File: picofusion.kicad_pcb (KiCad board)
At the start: 4 copper layers, 25.5 x 25.5 mm, 102 parts, among them J1 NORTH, J2 EAST, J3 WEST, J4 SOUTH, U1 W25Q16, U2 RP2040, U3 TLV71333PDQN, U4 ICM42605, U5 MMC5983MA, U6 ICP20100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

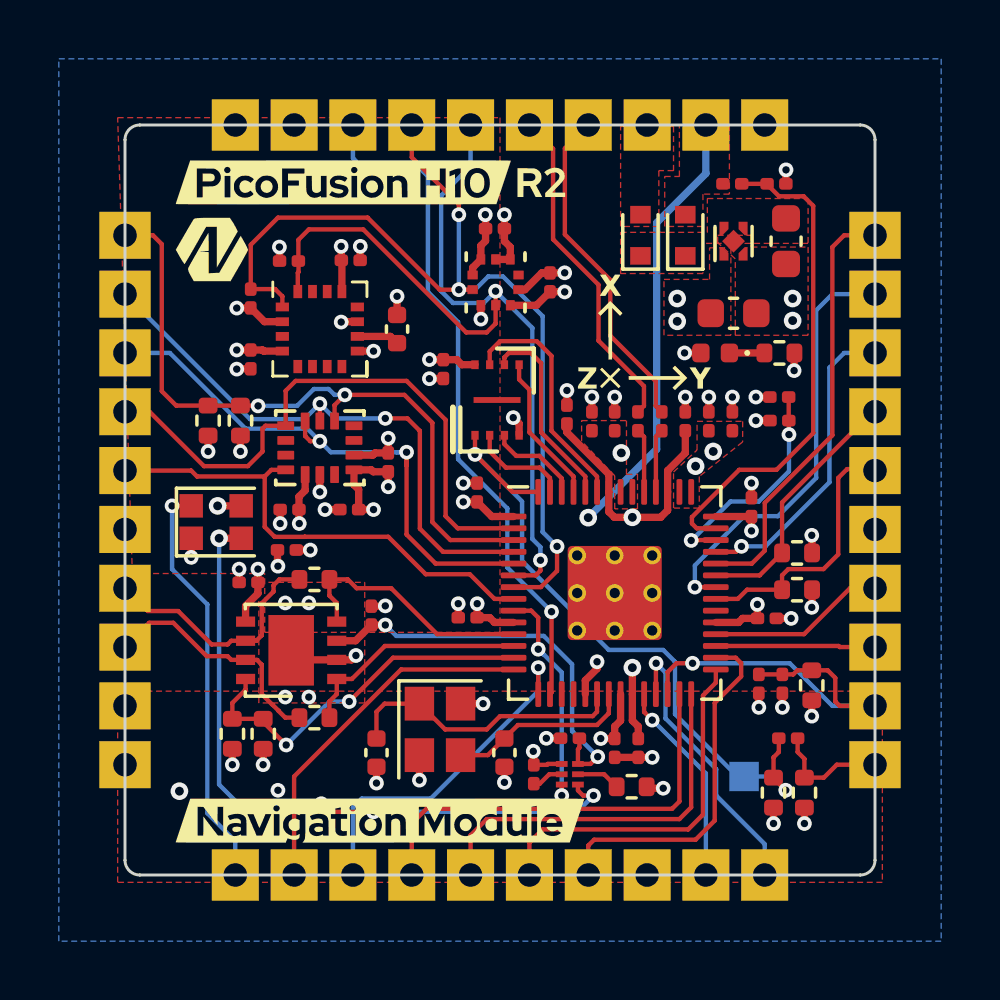
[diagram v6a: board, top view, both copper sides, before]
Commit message: schematic: reformat and R3 release candidate
* reformat schematic
* minor fixes from R2 testing
* no functionality differences
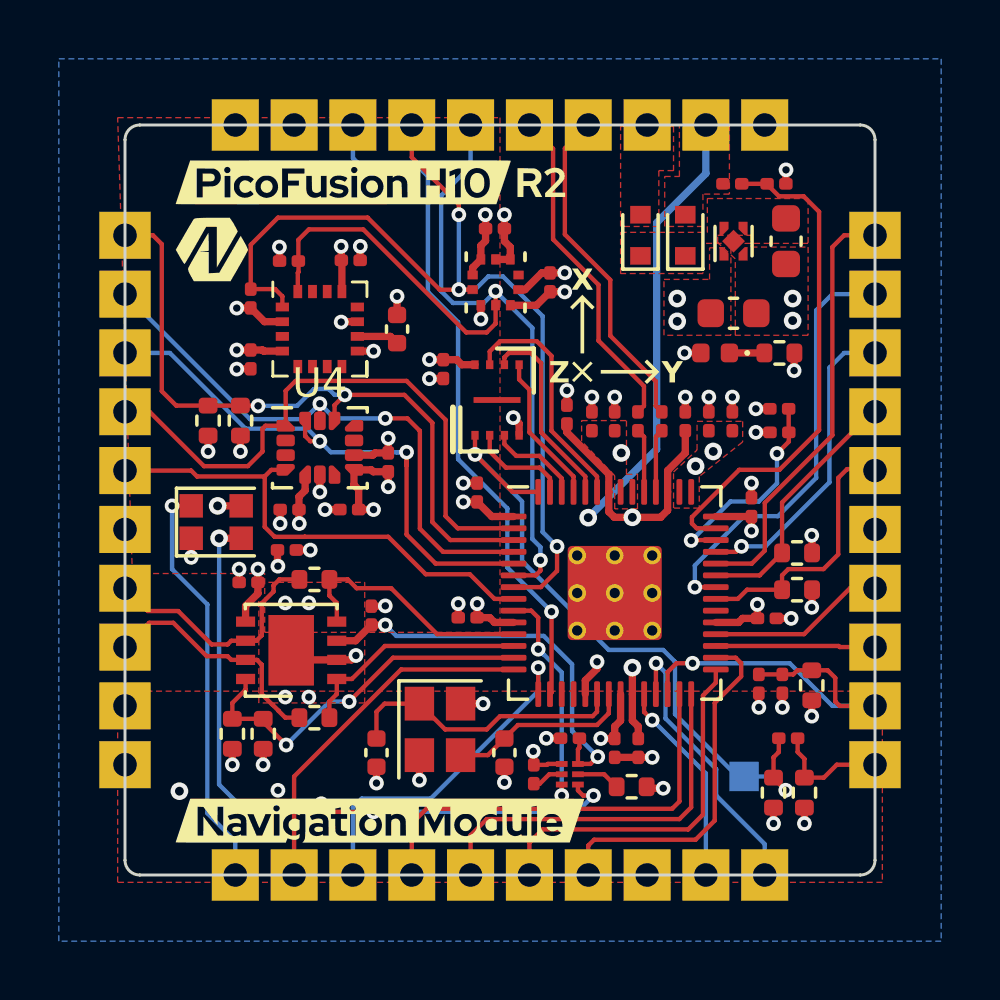
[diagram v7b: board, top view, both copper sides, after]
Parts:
- R6: value 470 -> 1.5K
- U4: footprint ICM-42605:PQFN50P300X250X97-14N -> Package_LGA:LGA-14_3x2.5mm_P0.5mm_LayoutBorder3x4y
- moved G*** 0.97 mm to (164.1, 34.4)
- moved R22 0.40 mm to (169.5, 37.7)
- moved R17 0.40 mm to (169.5, 36.9)
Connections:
- net /5V_RECT renamed Net-(C14-Pad1)
- net /LED_3V3 renamed /NEOPIXEL_3V3
- net /NEOPIXEL renamed Net-(D4-Pad3)
- net /QSPI_SCLK renamed /QSPI_SCK
- R15 pad 1: +5V -> +3V3
- R15 pad 2: /5V_SENSE -> /3V3_SENSE
- R16 pad 1: /5V_SENSE -> /3V3_SENSE
- R17 pad 1: +3V3 -> +5V
- R17 pad 2: /3V3_SENSE -> /5V_SENSE
- R22 pad 1: /3V3_SENSE -> /5V_SENSE
- U4 pad 10: unconnected-(U4-Pad10) -> (no net)
- U4 pad 11: unconnected-(U4-Pad11) -> (no net)
- U4 pad 2: unconnected-(U4-Pad2) -> (no net)
- U4 pad 3: unconnected-(U4-Pad3) -> (no net)
- U4 pad 7: unconnected-(U4-Pad7) -> (no net)
- U5 pad 12: (no net) -> unconnected-(U5-Pad12)
- U5 pad 14: (no net) -> unconnected-(U5-Pad14)
- U5 pad 3: (no net) -> unconnected-(U5-Pad3)
- U5 pad 6: (no net) -> unconnected-(U5-Pad6)
- U5 pad 7: (no net) -> unconnected-(U5-Pad7)
- U5 pad 8: (no net) -> unconnected-(U5-Pad8)
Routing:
- net /5V_SENSE: track 16.9 -> 7.27 mm, vias 0 -> 2
- net /3V3_SENSE: track 7.67 -> 17.1 mm, vias 2 -> 0
- net +5V: track 49.3 -> 49.8 mm, vias 5 -> 6
- net +3V3: track 33.9 -> 33.4 mm, vias 30 -> 29

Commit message: schematic: more improvements towards R3
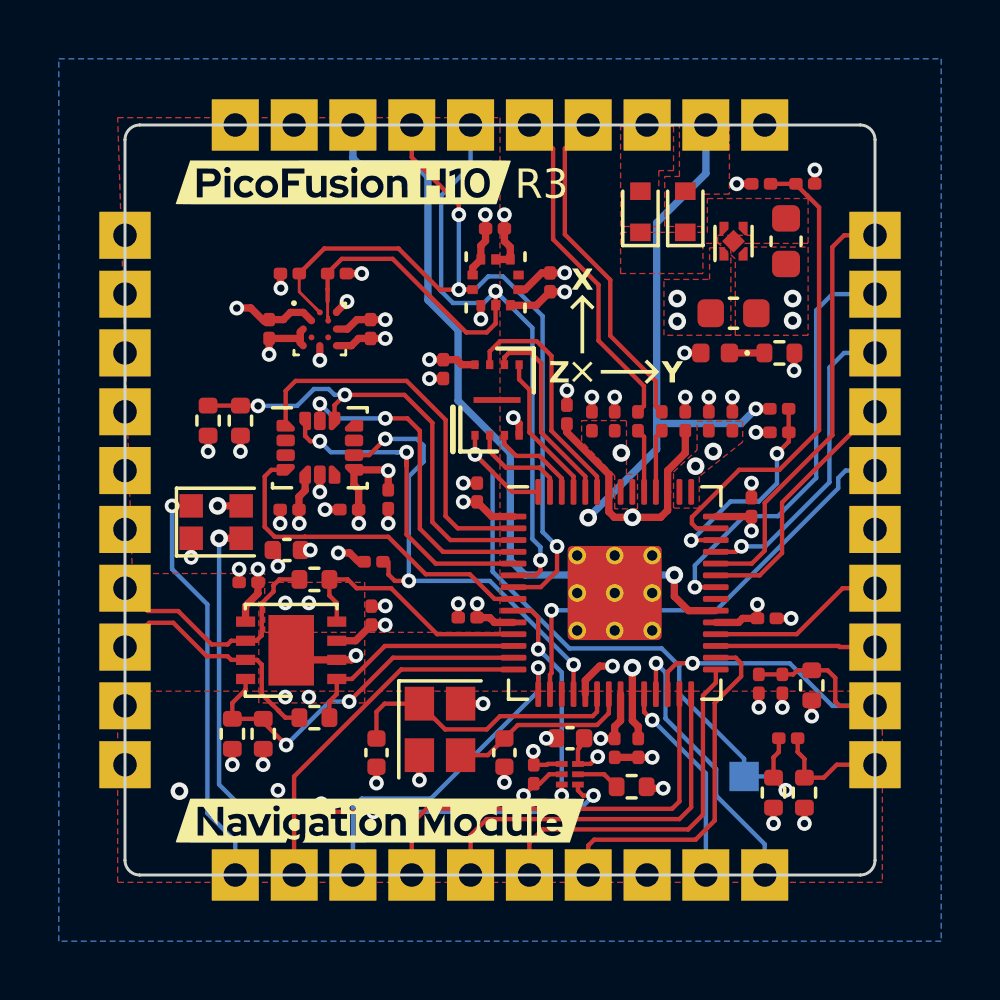
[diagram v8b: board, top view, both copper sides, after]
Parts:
- removed C12: 1uF, Capacitor_SMD:C_0201_0603Metric
- removed C20: 10uF, Capacitor_SMD:C_0402_1005Metric
- removed C21: 0.1uF, Capacitor_SMD:C_0201_0603Metric
- removed the G*** at (150.2, 31.5)
- removed the G*** at (157.0, 44.7)
- removed the G*** at (170.5, 29.2)
- removed R4, R5: 10K, Resistor_SMD:R_0402_1005Metric
- added C32: 0u1, Capacitor_SMD:C_0201_0603Metric, F.Cu at (152.2, 34.2)
- added C33: 0u1, Capacitor_SMD:C_0201_0603Metric, F.Cu at (155.6, 34.2)
- added R24: 10K, Resistor_SMD:R_0201_0603Metric, F.Cu at (155.7, 42.1)
- C1, C10, C11, C13, C14, C15, C16, C18, C2, C22, C23, C24, C26, C27, C28, C29, C4, C6, C7, C9: value 0.1uF -> 0u1
- C17: value 2.2uF -> 2u2
- C19: value 10nF -> 10n
- C25, C3: value 1uF -> 1u
- C30: value 0.1uF -> 0u1; footprint Capacitor_SMD:C_0201_0603Metric -> Capacitor_SMD:C_0402_1005Metric
- C31: value 1uF -> 1u; footprint Capacitor_SMD:C_0201_0603Metric -> Capacitor_SMD:C_0402_1005Metric
- C5, C8: value 10pF -> 10p
- R6, R8, R9: value 1.5K -> 1K5
- U4: value ICM42605 -> ICM-42688-P
- U5: value MMC5983MA -> BMM150; footprint Package_LGA:LGA-16_3x3mm_P0.5mm -> Package_CSP:WLCSP-12_1.56x1.56mm_P0.4mm
- moved R9 1.69 mm to (154.5, 32.3), turned to 180 degrees
- moved R8 1.58 mm to (152.9, 32.3), turned to 0 degrees
- moved C18 1.26 mm to (156.2, 40.0), turned to 90 degrees
- moved R15 0.98 mm to (168.9, 29.2)
- moved R16 0.98 mm to (170.4, 29.2)
- moved D1 0.80 mm to (166.3, 30.2)
- moved D3 0.80 mm to (164.8, 30.2)
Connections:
- net /SPI1_PICO_SD renamed /SPI1_MOSI
- net /SPI1_POCI_SD renamed /SPI1_MISO
- net /SPI1_SCK_SD renamed /SPI1_SCK
- net /SPI1_nCS_SD renamed /SPI1_nCS
- J1 pad 3: /RESV1 -> /USB_VBUS
- J2 pad 5: /SD_nCD -> /RESV1
- J3 pad 1: /SPI0_nCS -> unconnected-(J3-Pin_1-Pad1)
- J3 pad 2: /SPI0_SCK -> unconnected-(J3-Pin_2-Pad2)
- J3 pad 3: /SPI0_PICO -> unconnected-(J3-Pin_3-Pad3)
- J3 pad 4: /SPI0_POCI -> unconnected-(J3-Pin_4-Pad4)
- J3 pad 5: /DRDY_ICM42605 -> unconnected-(J3-Pin_5-Pad5)
- U2 pad 18: unconnected-(U2-Pad18) -> /PWM7B_FSYNC
- U2 pad 2: /SPI0_POCI -> /SPI0_MISO
- U2 pad 34: unconnected-(U2-Pad34) -> /USB_VBUS
- U2 pad 35: /SD_nCD -> unconnected-(U2-GPIO23-Pad35)
- U2 pad 40: /3V3_SENSE -> /5V_SENSE
- U2 pad 41: /5V_SENSE -> /3V3_SENSE
- U2 pad 5: /SPI0_PICO -> /SPI0_MOSI
- U2 pad 8: /DRDY_ICM42605 -> /DRDY_ICM42688P
- U4 pad 1: /SPI0_POCI -> /SPI0_MISO
- U4 pad 14: /SPI0_PICO -> /SPI0_MOSI
- U4 pad 4: /DRDY_ICM42605 -> /DRDY_ICM42688P
- U4 pad 9: GND -> /PWM7B_FSYNC
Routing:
- net /USB_VBUS: track 0.00 -> 26.2 mm, vias 0 -> 1
- net /SPI0_POCI: track 20.2 -> 0.00 mm
- net /SPI0_PICO: track 19.6 -> 0.00 mm, vias 2 -> 0
- net /DRDY_ICM42605: track 16.8 -> 0.00 mm
- net /PWM7B_FSYNC: track 0.00 -> 16.5 mm, vias 0 -> 3
- net /SPI0_MISO: track 0.00 -> 13.1 mm
- net /DRDY_ICM42688P: track 0.00 -> 12.0 mm
- net /SPI0_MOSI: track 0.00 -> 11.8 mm, vias 0 -> 2
- net /SD_nCD: track 8.98 -> 0.00 mm
- net /SPI0_SCK: track 19.7 -> 11.2 mm
- net /SPI0_nCS: track 23.8 -> 15.8 mm
- net /RESV1: track 23.2 -> 16.0 mm
- net +5V: track 49.8 -> 54.5 mm
- net /I2C0_SCL: track 32.3 -> 29.0 mm
- net GND: track 32.1 -> 34.3 mm
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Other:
- board text added: "R3"
